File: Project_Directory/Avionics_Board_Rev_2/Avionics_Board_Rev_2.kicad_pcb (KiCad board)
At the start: 2 copper layers, 60 x 130 mm, 86 parts, among them J1 Battery, J10 PWM_1, J11 PWM_2, J12 PWM_3, J13 I2C, J14 UART, J15 Conn_Coaxial, J16 ON, J2 ARM, J3 PYRO_1, J4 PYRO_3, J5 PYRO_2, J6 PYRO_4, J7 PWM_4, J8 PWM_5, J9 PWM_6, Q1 Drive_MOS, Q2 Drive_MOS, Q3 Drive_MOS, Q4 Drive_MOS, Q5 Drive_MOS, SW1 SW_DPDT_x2, U1 Teensy4.1, U10 GSM, U11 AP2127K-3.3, U2 LoRa - RFM95-W/PW, U3 ADXL, U4 ADS1115IDGS, U5 AMS1117-3.3, U6 GPS, U7 GY-91, U8 AMS1117-5.0

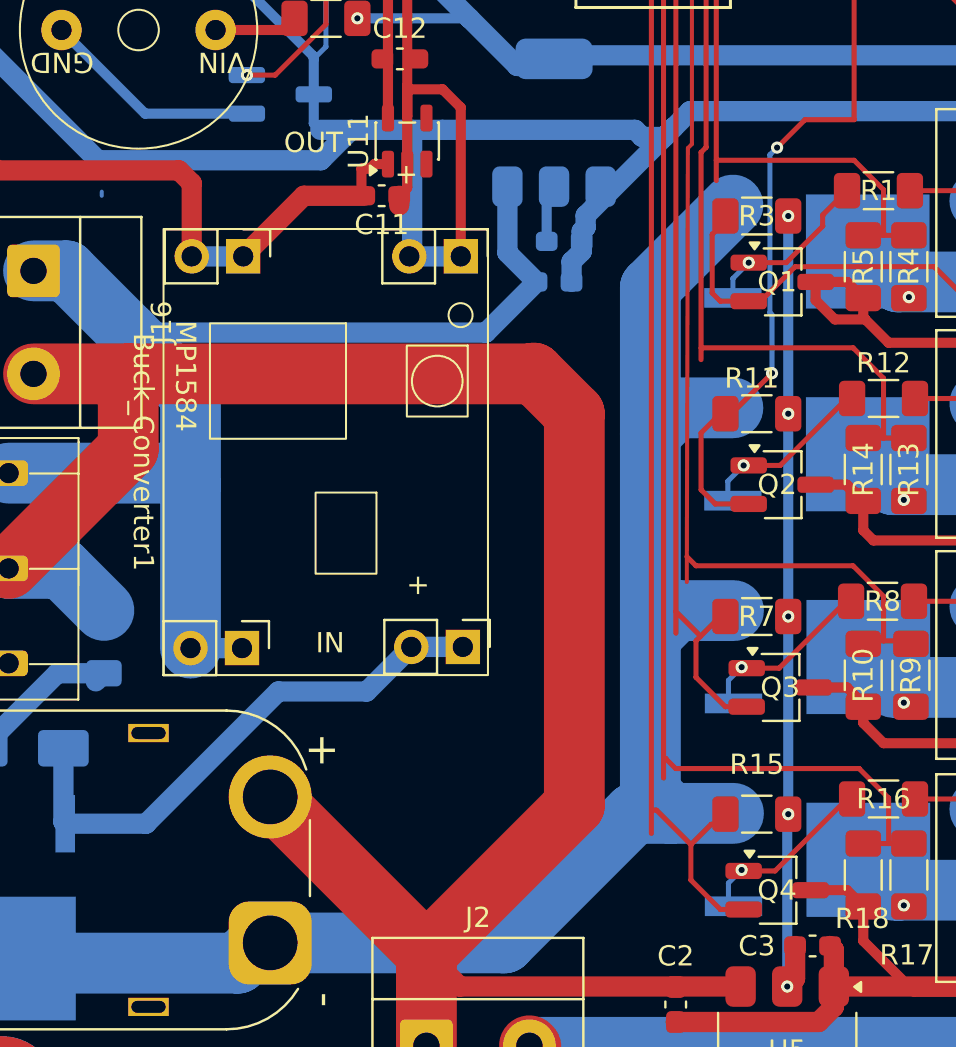
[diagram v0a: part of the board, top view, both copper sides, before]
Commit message: corrected buckconverter and drive mos
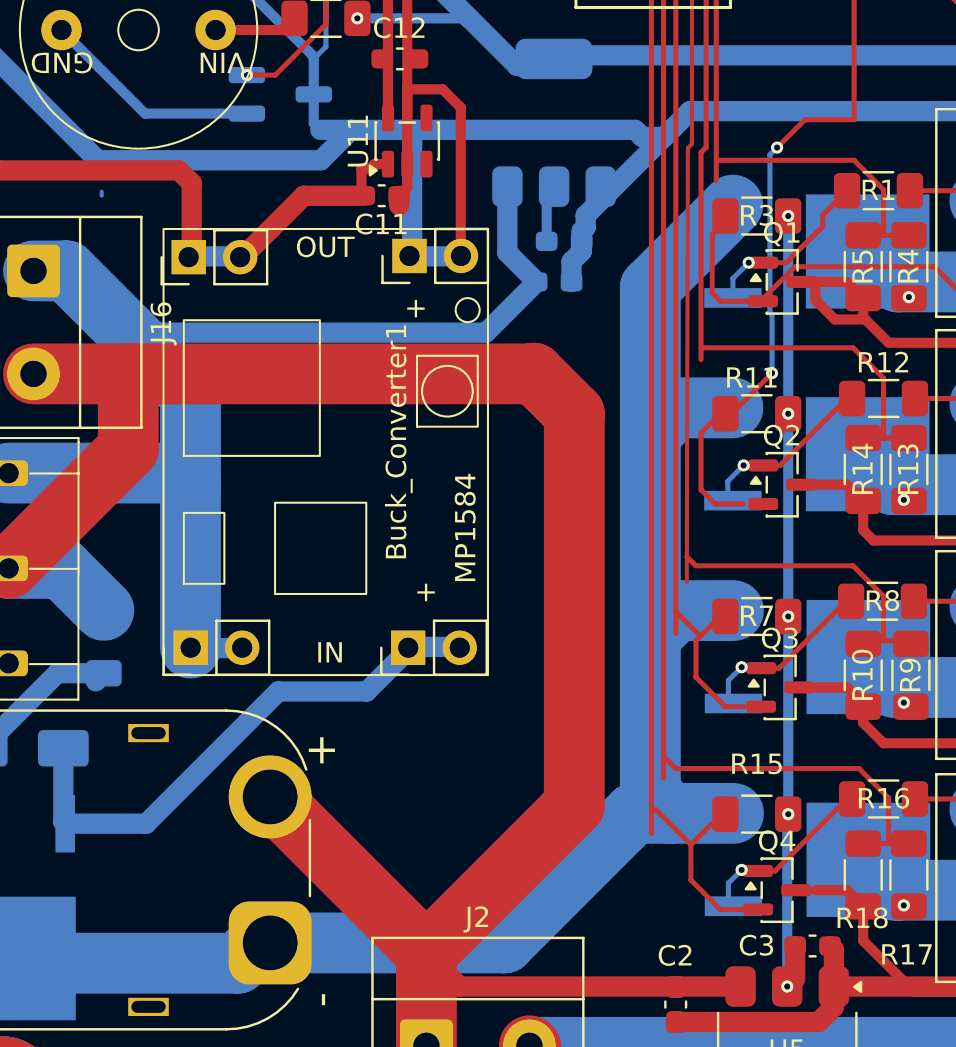
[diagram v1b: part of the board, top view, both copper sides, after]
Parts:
- Buck_Converter1: footprint VelR:buck converter -> VelR:buck converter_corrected
- Q1, Q2, Q3, Q4: footprint Package_TO_SOT_SMD:SC-59_Handsoldering -> Package_TO_SOT_SMD:SOT-23
- turned Buck_Converter1 to 90 degrees
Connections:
- Buck_Converter1 pad 1: GND -> /GND_PWR
- Buck_Converter1 pad 2: GND -> /GND_PWR
- Buck_Converter1 pad 3: /BUCK_Out -> +BATT_C
- Buck_Converter1 pad 4: /BUCK_Out -> +BATT_C
- Buck_Converter1 pad 5: +BATT_C -> /BUCK_Out
- Buck_Converter1 pad 6: +BATT_C -> /BUCK_Out
- Buck_Converter1 pad 7: /GND_PWR -> GND
- Buck_Converter1 pad 8: /GND_PWR -> GND
- C1 pad 1: Net-(Q1-D) -> Net-(Q1-S)
- C10 pad 1: Net-(Q4-D) -> Net-(Q4-S)
- C8 pad 1: Net-(Q3-D) -> Net-(Q3-S)
- C9 pad 1: Net-(Q2-D) -> Net-(Q2-S)
- Q1 pad 1: Net-(Q1-D) -> /PYRO_1_Trig
- Q1 pad 2: /PYRO_1_Trig -> GND
- Q1 pad 3: GND -> Net-(Q1-S)
- Q2 pad 1: Net-(Q2-D) -> /PYRO_2_Trig
- Q2 pad 2: /PYRO_2_Trig -> GND
- Q2 pad 3: GND -> Net-(Q2-S)
- Q3 pad 1: Net-(Q3-D) -> /PYRO_3_Trig
- Q3 pad 2: /PYRO_3_Trig -> GND
- Q3 pad 3: GND -> Net-(Q3-S)
- Q4 pad 1: Net-(Q4-D) -> /PYRO_4_Trig
- Q4 pad 2: /PYRO_4_Trig -> GND
- Q4 pad 3: GND -> Net-(Q4-S)
- R1 pad 2: Net-(Q1-D) -> Net-(Q1-S)
- R12 pad 2: Net-(Q2-D) -> Net-(Q2-S)
- R16 pad 2: Net-(Q4-D) -> Net-(Q4-S)
- R8 pad 2: Net-(Q3-D) -> Net-(Q3-S)

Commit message: patch work 5 march
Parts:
- moved Q2 1.48 mm to (163.0, 121.9), turned to -90 degrees
- moved Q1 1.36 mm to (163.1, 112.0), turned to -90 degrees
- moved Q3 1.18 mm to (163.2, 131.9), turned to -90 degrees
- moved Q4 1.03 mm to (163.2, 141.9), turned to -90 degrees
- moved R3 0.20 mm to (163.2, 108.8)
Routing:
- net GND: track 559.8 -> 600.7 mm
- net /PYRO_1_Trig: track 53.9 -> 41.3 mm
- net Net-(Q1-D): track 8.71 -> 0.00 mm, vias 1 -> 0
- net Net-(Q4-D): track 8.63 -> 0.00 mm, vias 1 -> 0
- net Net-(Q2-D): track 8.53 -> 0.00 mm, vias 1 -> 0
- net Net-(Q3-D): track 8.48 -> 0.00 mm, vias 1 -> 0
- net Net-(Q3-S): track 0.00 -> 8.32 mm, vias 0 -> 1
- net Net-(Q2-S): track 0.00 -> 8.21 mm, vias 0 -> 1
- net Net-(Q1-S): track 0.00 -> 7.96 mm, vias 0 -> 1
- net Net-(Q4-S): track 0.00 -> 7.91 mm, vias 0 -> 1
- net /GND_PWR: track 27.0 -> 19.9 mm
- net +BATT_C: track 61.0 -> 67.0 mm
- net /PYRO_4_Trig: track 63.5 -> 58.6 mm
- net /PYRO_3_Trig: track 57.9 -> 54.1 mm
- net /PYRO_2_Trig: track 36.9 -> 33.6 mm
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
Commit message: modification 1 7 mmarch
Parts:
- removed REF** (x4): MountingHole_3.2mm_M3_DIN965_Pad_TopBottom, MountingHole:MountingHole_3.2mm_M3_DIN965_Pad_TopBottom
- added G***: LOGO, VelR:VelR logo 1.5_2cm, F.Cu at (135.6, 58.3)
- added H1: MountingHole_Pad, MountingHole:MountingHole_3.2mm_M3_DIN965_Pad_TopBottom, F.Cu at (125.8, 40.7)
- added H2: MountingHole_Pad, MountingHole:MountingHole_3.2mm_M3_DIN965_Pad_TopBottom, F.Cu at (125.8, 152.2)
- added H3: MountingHole_Pad, MountingHole:MountingHole_3.2mm_M3_DIN965_Pad_TopBottom, F.Cu at (179.8, 35.7)
- added H4: MountingHole_Pad, MountingHole:MountingHole_3.2mm_M3_DIN965_Pad_TopBottom, F.Cu at (179.8, 152.2)
- Q5: footprint Package_TO_SOT_SMD:SC-59_Handsoldering -> Package_TO_SOT_SMD:SOT-23
- moved U6 6.38 mm to (174.0, 48.0), turned to 0 degrees
- moved J6 2.80 mm to (177.4, 141.3)
- moved U10 2.02 mm to (177.4, 29.9)
- moved J4 1.80 mm to (177.4, 131.3)
- moved LED1 1.26 mm to (169.7, 84.0)
- moved C9 1.11 mm to (166.1, 119.6)
- moved D4 1.11 mm to (174.2, 119.1)
- moved Q2 1.11 mm to (163.0, 120.8)
- moved R11 1.11 mm to (163.2, 117.6)
- moved R12 1.11 mm to (169.4, 116.8)
- moved R13 1.11 mm to (170.7, 120.3)
- moved R14 1.11 mm to (168.4, 120.3)
- moved Q5 1.06 mm to (138.9, 103.7), turned to 180 degrees
- moved J15 1.00 mm to (132.2, 27.4)
- moved C10 0.95 mm to (166.2, 139.8)
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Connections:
- Q5 pad 1: Net-(BZ1-GND) -> /Buzzer
- Q5 pad 2: /Buzzer -> GND
- Q5 pad 3: GND -> Net-(BZ1-GND)
- U1 pad 2: /PYRO_2_Trig -> /PYRO_1_Trig
- U1 pad 3: /PYRO_1_Trig -> /PYRO_2_Trig
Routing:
- net /PYRO_3_continuity: track 28.4 -> 62.9 mm
- net /SPI1_SCK: track 25.7 -> 47.7 mm
- net GND: track 600.7 -> 579.0 mm, vias 17 -> 24
- net /PYRO_1_Trig: track 41.3 -> 22.3 mm, vias 0 -> 2
- net +3.3V: track 201.1 -> 211.8 mm, vias 0 -> 4
- net +BATT: track 109.9 -> 104.1 mm
- net +BATT_C: track 67.0 -> 72.1 mm
- net +VDC: track 128.6 -> 124.1 mm
- net +5V: track 129.7 -> 132.8 mm, vias 4 -> 5
- net /GPS_RX: track 14.3 -> 11.2 mm
- net /GSM_RX: track 32.5 -> 30.0 mm
- net /GSM_TX: track 28.5 -> 26.2 mm
- net /GSM_RST: track 24.8 -> 22.7 mm
- net /GPS_TX: track 13.7 -> 11.6 mm
- net /BUCK_Out: track 151.5 -> 149.7 mm
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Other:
- board size 60 x 130 mm -> 60.1 x 130 mm
- board text added: "1 2 3 4 5 6"
- board text added: "ARM"
- board text added: "GSM-gnd rst tx rx v"
- board text added: "I2C-gnd sda scl vcc"
- board text added: "PWM"
- board text added: "PYRO"
- board text added: "Power"
- board text added: "UART-gnd rx tx vcc"
- board text added: "W PW"
- board text added: "put kapton tape on for isolation"
- board text added: "pyro - 1"
- board text added: "pyro - 2"
- board text added: "pyro - 3"
- board text added: "pyro - 4"
- board text added: "{dblquote}Vetrivel Muruganukku Arogara{dblquote}"

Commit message: Modification 2 march 7
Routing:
- net /BUCK_Out: track 149.7 -> 155.4 mm
- net GND: track 579.0 -> 583.2 mm
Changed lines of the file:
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@@
 	)
 	(segment
+		(start 146.55 109.2)
+		(end 143.8875 109.2)
+		(width 0.5)
+		(layer "F.Cu")
+		(net 4)
+	)
+	(segment
 		(start 144.55 111)
 		(end 144.63 110.92)
@@
 	)
 	(segment
+		(start 146.909001 106.3895)
+		(end 146.909001 108.840999)
+		(width 0.5)
+		(layer "F.Cu")
+		(net 4)
+	)
+	(segment
 		(start 135.95 107.95)
 		(end 143.8375 107.95)
@@
 	)
 	(segment
-		(start 143.8375 107.95)
+		(start 143.8375 109.25)
 		(end 143.8375 110.2875)
 		(width 1)
@@
 	)
 	(segment
+		(start 146.909001 108.840999)
+		(end 146.55 109.2)
+		(width 0.5)
+		(layer "F.Cu")
+		(net 4)
+	)
+	(segment
 		(start 134.7 106.7)
 		(end 135.95 107.95)
@@
 	)
 	(segment
+		(start 143.8875 109.2)
+		(end 143.8375 109.25)
+		(width 0.5)
+		(layer "F.Cu")
+		(net 4)
+	)
+	(segment
 		(start 143.701001 107.676001)
 		(end 143.725 107.7)
@@
 		(net 4)
 	)
+	(segment
+		(start 143.8375 107.95)
+		(end 143.8375 109.25)
+		(width 1)
+		(layer "F.Cu")
+		(net 4)
+	)
 	(via
 		(at 148.7 34.2)
@@
 	)
 	(segment
-		(start 146.7 108.2)
-		(end 146.45 107.95)
+		(start 180.45925 117.4)
+		(end 180.45925 115.6)
 		(width 1)
 		(layer "F.Cu")
@@
 	)
 	(segment
-		(start 180.45925 117.4)
-		(end 180.45925 115.6)
+		(start 152.2 111.45)
+		(end 152.2 109.45)
 		(width 1)
 		(layer "F.Cu")
@@
 	)
 	(segment
-		(start 137.48 110.98)
-		(end 140.45 113.95)
+		(start 148 101.2)
+		(end 146.458 101.2)
 		(width 1)
 		(layer "F.Cu")
@@
 	)
 	(segment
-		(start 149.7 113.95)
-		(end 152.2 111.45)
-		(width 1)
-		(layer "F.Cu")
-		(net 5)
-	)
-	(segment
 		(start 168 41.535)
 		(end 165.189818 41.535)
@@
 	)
 	(segment
-		(start 150.95 108.2)
-		(end 146.7 108.2)
-		(width 1)
-		(layer "F.Cu")
-		(net 5)
-	)
-	(segment
 		(start 178.65125 123.8)
 		(end 180.45125 125.6)
@@
 	)
 	(segment
-		(start 146.45 107.95)
-		(end 145.5625 107.95)
-		(width 1)
-		(layer "F.Cu")
-		(net 5)
-	)
-	(segment
 		(start 168.4 113.9)
 		(end 163.1 113.9)
@@
 	)
 	(segment
+		(start 150.95 108.15)
+		(end 148.95 106.15)
+		(width 1)
+		(layer "F.Cu")
+		(net 5)
+	)
+	(segment
 		(start 163.3 133.8)
 		(end 162.25 132.75)
@@
 	)
 	(segment
+		(start 137.48 110.98)
+		(end 140.45 113.95)
+		(width 1)
+		(layer "F.Cu")
+		(net 5)
+	)
+	(segment
 		(start 145.959001 107.553499)
 		(end 145.5625 107.95)
@@
 	)
 	(segment
+		(start 140.45 113.95)
+		(end 149.7 113.95)
+		(width 1)
+		(layer "F.Cu")
+		(net 5)
+	)
+	(segment
 		(start 180.45125 126.69875)
 		(end 180.45 126.7)
@@
 	)
 	(segment
-		(start 135.18 110.98)
-		(end 137.48 110.98)
-		(width 1)
-		(layer "F.Cu")
-		(net 5)
-	)
-	(segment
 		(start 146.213205 52.086795)
 		(end 146.213205 52.648631)
@@
 	)
 	(segment
+		(start 135.18 110.98)
+		(end 137.48 110.98)
+		(width 1)
+		(layer "F.Cu")
+		(net 5)
+	)
+	(segment
 		(start 162.649818 44.075)
 		(end 170.665 44.075)
@@
 	)
 	(segment
+		(start 148.95 106.15)
+		(end 148.95 102.15)
+		(width 1)
+		(layer "F.Cu")
+		(net 5)
+	)
+	(segment
 		(start 168.4 111.825)
 		(end 168.4 113.9)
@@
 	)
 	(segment
-		(start 152.2 111.45)
-		(end 152.2 109.45)
-		(width 1)
-		(layer "F.Cu")
-		(net 5)
-	)
-	(segment
 		(start 169.1 133.8)
 		(end 163.3 133.8)
@@
 	)
 	(segment
+		(start 148.95 102.15)
+		(end 148 101.2)
+		(width 1)
+		(layer "F.Cu")
+		(net 5)
+	)
+	(segment
 		(start 162.25 143.15)
 		(end 162.25 140.0625)
@@
 	)
 	(segment
-		(start 180.45 126.7)
-		(end 180.45 135.2)
+		(start 149.7 113.95)
+		(end 152.2 111.45)
 		(width 1)
 		(layer "F.Cu")
@@
 	)
 	(segment
-		(start 140.45 113.95)
-		(end 149.7 113.95)
+		(start 180.45 126.7)
+		(end 180.45 135.2)
 		(width 1)
 		(layer "F.Cu")
@@
 		(net 5)
 	)
+	(segment
+		(start 150.95 108.2)
+		(end 150.95 108.15)
+		(width 1)
+		(layer "F.Cu")
+		(net 5)
+	)
 	(via
 		(at 146.458 60.566)
@@
 		(net 5)
 		(net_name "GND")
-		(locked yes)
 		(layer "F.Cu")
 		(hatch edge 0.5)
+		(connect_pads yes
+			(clearance 0.15)
+		)
+		(min_thickness 0.25)
+		(filled_areas_thickness no)
+		(fill yes
+			(thermal_gap 0.5)
+			(thermal_bridge_width 0.5)
+		)
+		(polygon
+			(pts
+				(xy 121.65 21.45) (xy 143.9 21.35) (xy 145.2 21.4) (xy 145.3 36) (xy 148.65 36.25) (xy 148.6 71.85)
+				(xy 144.4 75.55) (xy 120.65 75.7)
+			)
+		)
+	)
+	(zone
+		(net 5)
+		(net_name "GND")
+		(layer "F.Cu")
+		(hatch edge 0.5)
+		(priority 3)
 		(connect_pads
 			(clearance 0.5)
@@
 		(polygon
 			(pts
-				(xy 118.6 16.6) (xy 126.8 12.8) (xy 189.2 16.8) (xy 189.4 154.4) (xy 174.2 164) (xy 116.4 161.6)
+				(xy 145.2 21.4) (xy 145.2 48.2) (xy 148.5 51.9) (xy 149 75.05) (xy 120.65 75.7) (xy 120.3 157.5)
+				(xy 184.55 158.55) (xy 184.45 22.2)
 			)
 		)

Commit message: Modification 3 7th march
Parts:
- added R27: 2.2k, Resistor_SMD:R_1206_3216Metric_Pad1.30x1.75mm_HandSolder, B.Cu at (173.2, 59.5)
- added R28: 2.2k, Resistor_SMD:R_1206_3216Metric_Pad1.30x1.75mm_HandSolder, B.Cu at (176.2, 59.5)
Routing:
- net +3.3V: track 211.8 -> 222.6 mm
- net /Spare_I2C_SDA: track 9.34 -> 12.5 mm
- net /Spare_I2C_SCL: track 11.7 -> 14.6 mm

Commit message: QR added
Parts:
- added G***: LOGO, Library:QR#, B.Cu at (141.8, 120.5)

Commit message: asthetics
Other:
- board text added: "Telemetry gossip port"
- board text added: "WARNING: Pointy end up, Flamey end down"
- board text added: "if found return to 13°43'06.7{dblquote}N 79°35'18.9{dblquote}E"
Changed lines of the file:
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@@
 			(psa4output no)
 			(plot_black_and_white yes)
+			(plotinvisibletext no)
 			(sketchpadsonfab no)
 			(plotpadnumbers no)
@@
 		)
 		(fp_text user "3.3/5v"
-			(at 21.12 1.67 270)
+			(at 21.086 4.792 0)
 			(unlocked yes)
 			(layer "B.SilkS")
@@
 		(layer "Edge.Cuts")
 	)
+	(gr_text "WARNING:\nPointy end up, Flamey end down"
+		(at 157 139.25 90)
+		(layer "F.SilkS")
+		(effects
+			(font
+				(size 1.5 1.5)
+				(thickness 0.25)
+				(bold yes)
+			)
+			(justify left bottom)
+		)
+	)
 	(gr_text "PYRO\n"
 		(at 174.4 103.4 0)
@@
 		)
 	)
+	(gr_text "if found return to\n13°43'06.7{dblquote}N 79°35'18.9{dblquote}E"
+		(at 163.72 30.44 0)
+		(layer "B.SilkS")
+		(effects
+			(font
+				(size 1 1)
+				(thickness 0.25)
+				(bold yes)
+			)
+			(justify left bottom mirror)
+		)
+	)
+	(gr_text "Telemetry gossip port"
+		(at 146.97 34.34 0)
+		(layer "B.SilkS")
+		(effects
+			(font
+				(size 0.7 0.7)
+				(thickness 0.175)
+				(bold yes)
+			)
+			(justify left bottom mirror)
+		)
+	)

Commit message: final additions , v-2.0.0
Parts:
- added G***: LOGO, VelR:Vel, B.Cu at (158.2, 64.4)
- moved G*** 3.43 mm to (138.8, 57.0)
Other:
- board text added: "Avionics V-2.0.0"
- board text added: "Sky's no limit !"
- board text added: "WARNING: Pointy end up, Flamy end down"
- board text added: "if found return to 13°43'06.7{dblquote}N 79°35'18.9{dblquote}E TEL : 0877-250-3041"
- board text removed: "WARNING: Pointy end up, Flamey end down"
- board text removed: "if found return to 13°43'06.7{dblquote}N 79°35'18.9{dblquote}E"
